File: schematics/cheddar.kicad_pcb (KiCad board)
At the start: 2 copper layers, 43 x 26 mm, 30 parts, among them J1 USB_OTG, J2 Conn_01x08, J3 Conn_01x08, J4 EXTERNAL_TRIGGER, J5 BATT_CONN, Q1 MOSFET_PCH, SW1 SW_Push, U1 CH340G, U2 MCP73831, U3 ESP-12E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

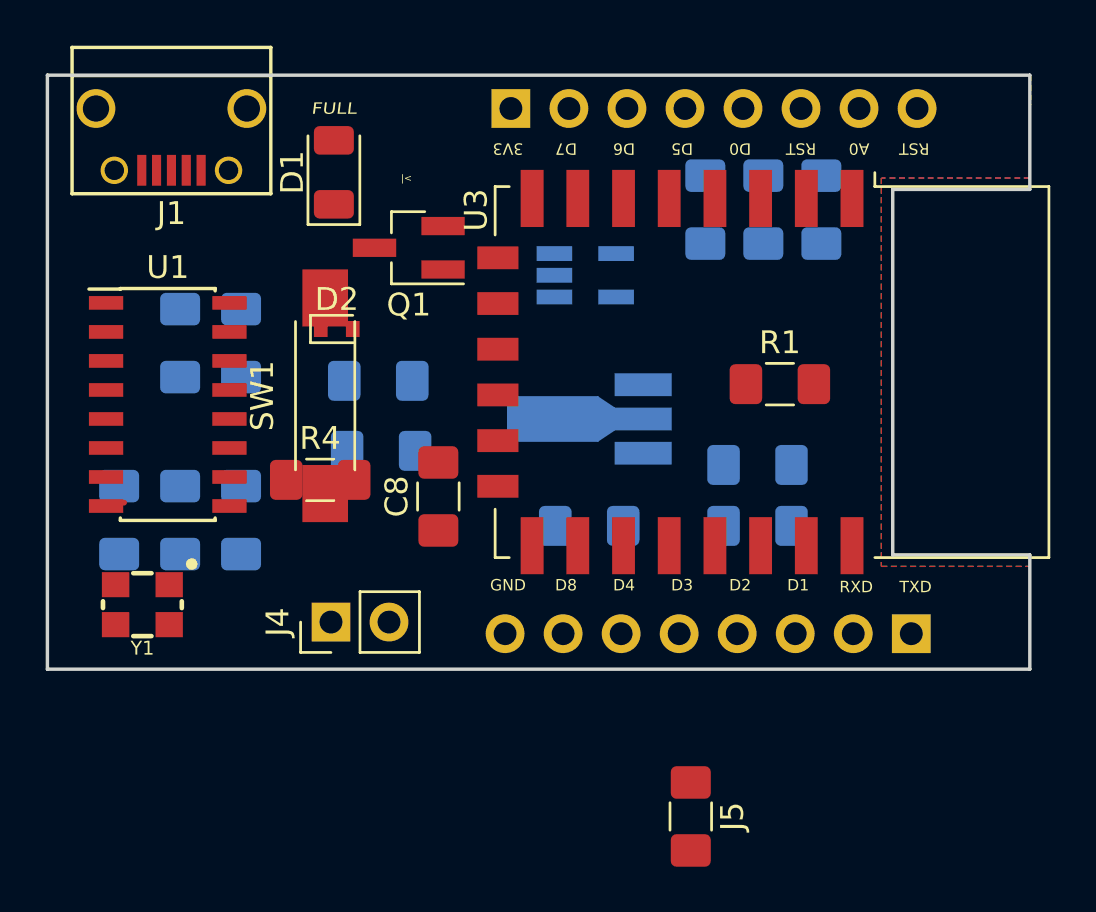
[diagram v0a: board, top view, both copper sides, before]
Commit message: Routed new PCB
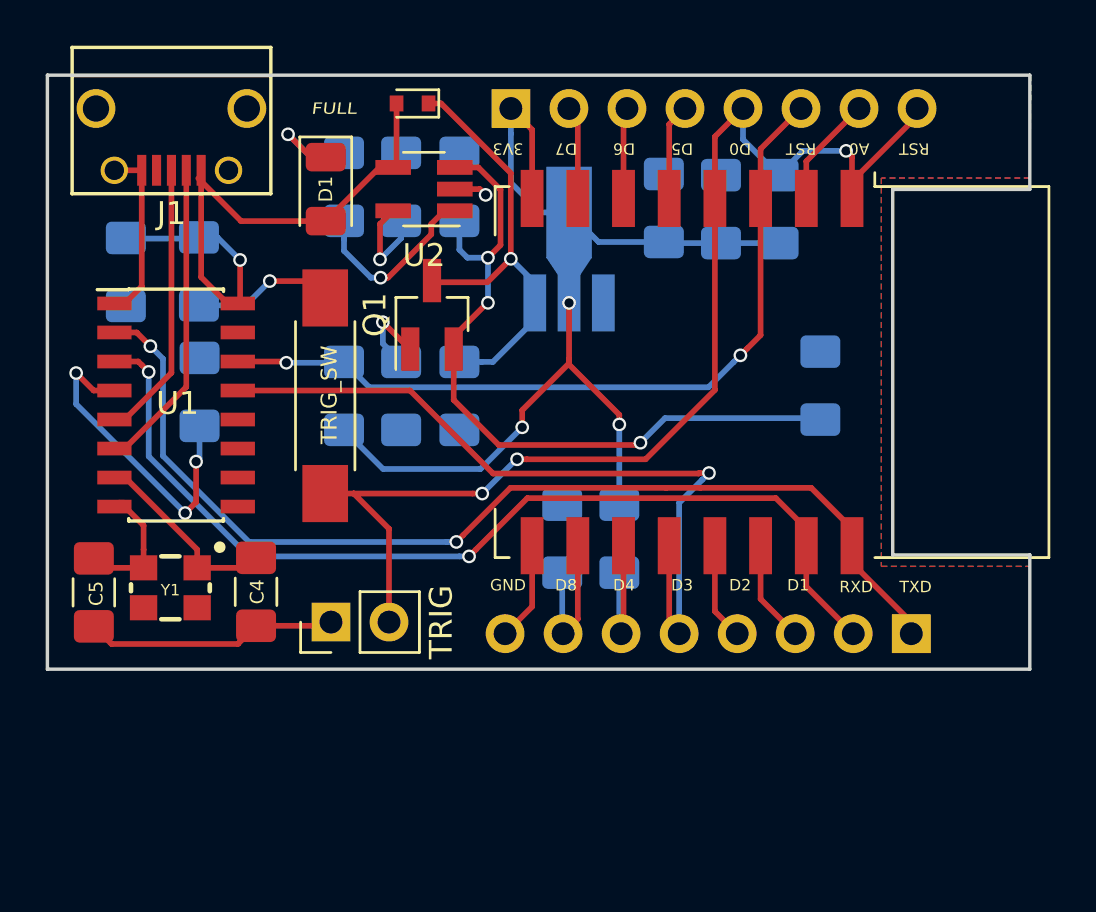
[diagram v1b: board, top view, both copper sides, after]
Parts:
- C4, C5, U2: moved to F.Cu
- C8, J5, R1, R4: moved to B.Cu
- moved C1 24.9 mm to (139.0, 99.0)
- moved C6 24.4 mm to (161.8, 96.2), turned to 270 degrees
- moved C7 19.8 mm to (150.4, 95.2), turned to 270 degrees
- moved J5 19.7 mm to (166.2, 104.0)
- moved R2 19.1 mm to (164.4, 96.2), turned to 90 degrees
- moved R1 18.7 mm to (147.8, 95.2), turned to 90 degrees
- moved R5 18.3 mm to (154.9, 110.7), turned to 90 degrees
- moved R3 15.8 mm to (145.3, 95.2), turned to 90 degrees
- moved C9 12.0 mm to (159.3, 96.2), turned to 90 degrees
- moved C2 11.1 mm to (135.8, 99.0), turned to 90 degrees
- moved C4 10.9 mm to (141.5, 113.0), turned to 270 degrees
- moved ? 10.4 mm to (148.3, 91.6), turned to 180 degrees
- moved U2 8.00 mm to (148.8, 95.3), turned to 180 degrees
- moved C5 7.18 mm to (134.4, 113.0), turned to 270 degrees
- moved U4 7.17 mm to (155.2, 98.3), turned to 90 degrees
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- renumbered U3 to ?, D2 to ?, J2 to ?, J4 to TRIG, SW1 to TRIG_SW
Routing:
- net /GPIO16: track 0.00 -> 52.3 mm, vias 0 -> 3
- net +3V3: track 0.00 -> 47.9 mm, vias 0 -> 3
- net /TXD: track 0.00 -> 46.0 mm, vias 0 -> 2
- net /RXD: track 0.00 -> 43.0 mm, vias 0 -> 2
- net /CH_PD: track 0.00 -> 35.1 mm, vias 0 -> 2
- net /GPIO0: track 0.00 -> 33.7 mm, vias 0 -> 1
- net Net-(C7-Pad2): track 0.00 -> 32.5 mm, vias 0 -> 3
- net +5V: track 0.00 -> 31.0 mm, vias 0 -> 2
- net GND: track 0.00 -> 30.9 mm, vias 0 -> 2
- net Net-(C8-Pad1): track 0.00 -> 19.7 mm, vias 0 -> 1
- net Net-(C3-Pad1): track 0.00 -> 14.6 mm, vias 0 -> 3
- net /D-: track 0.00 -> 13.7 mm
- net /D+: track 0.00 -> 12.2 mm
- net /XI: track 0.00 -> 8.49 mm
- net Net-(R3-Pad1): track 0.00 -> 8.13 mm, vias 0 -> 1
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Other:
- board text removed: "|<"
